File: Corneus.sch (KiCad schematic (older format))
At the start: 145 parts, among them J1 USB_B_Micro, Q1 Q_NPN_BCE, SW1 SW_Push, U1 ATmega32U4-AU, U2 PRTR5V0U2X, Y1 16MHz

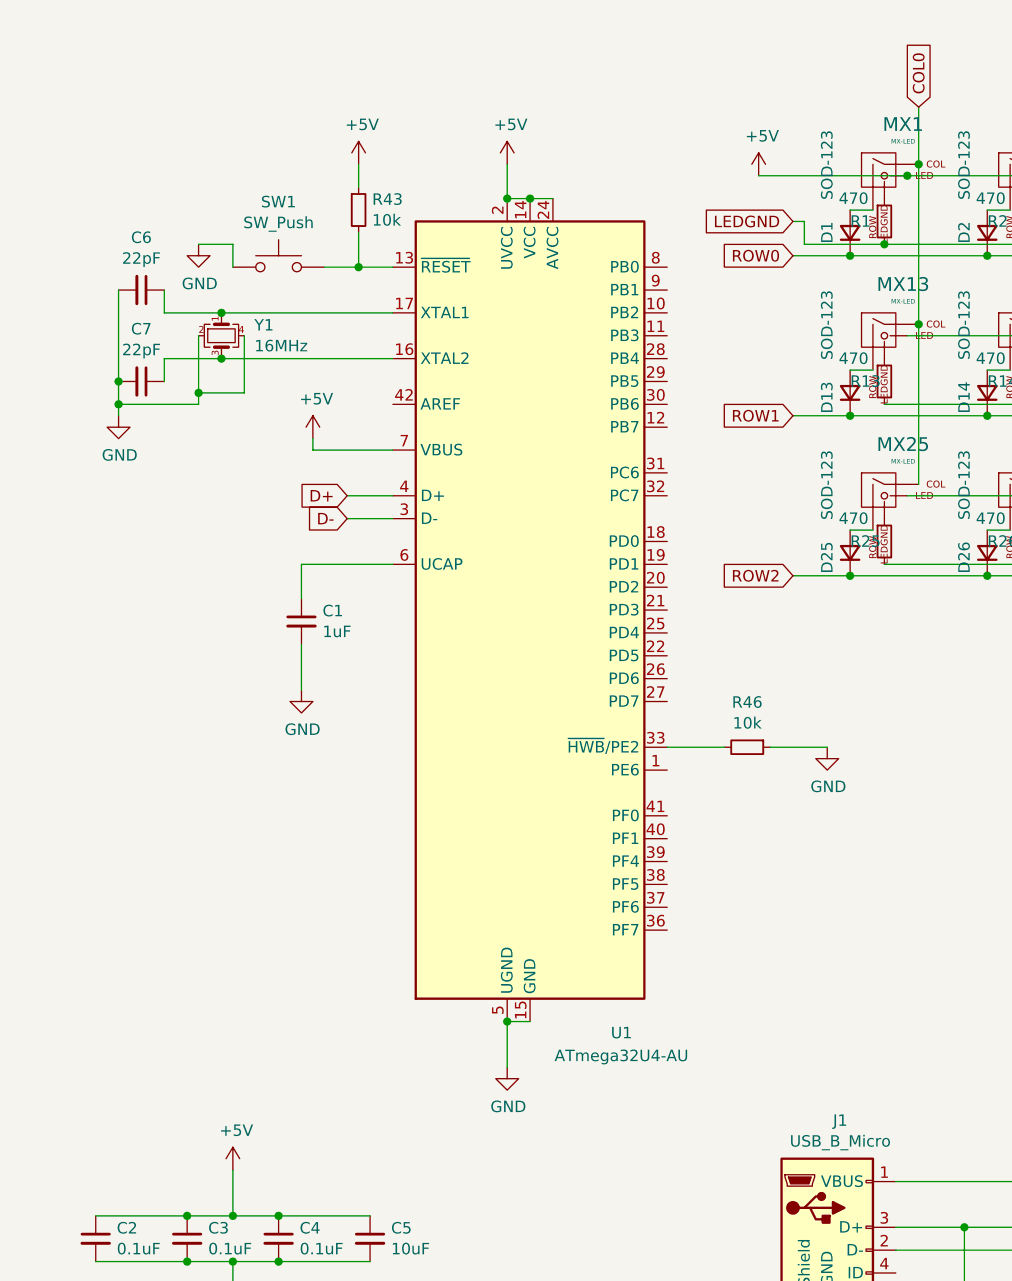
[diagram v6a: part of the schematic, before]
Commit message: routed rows and columns
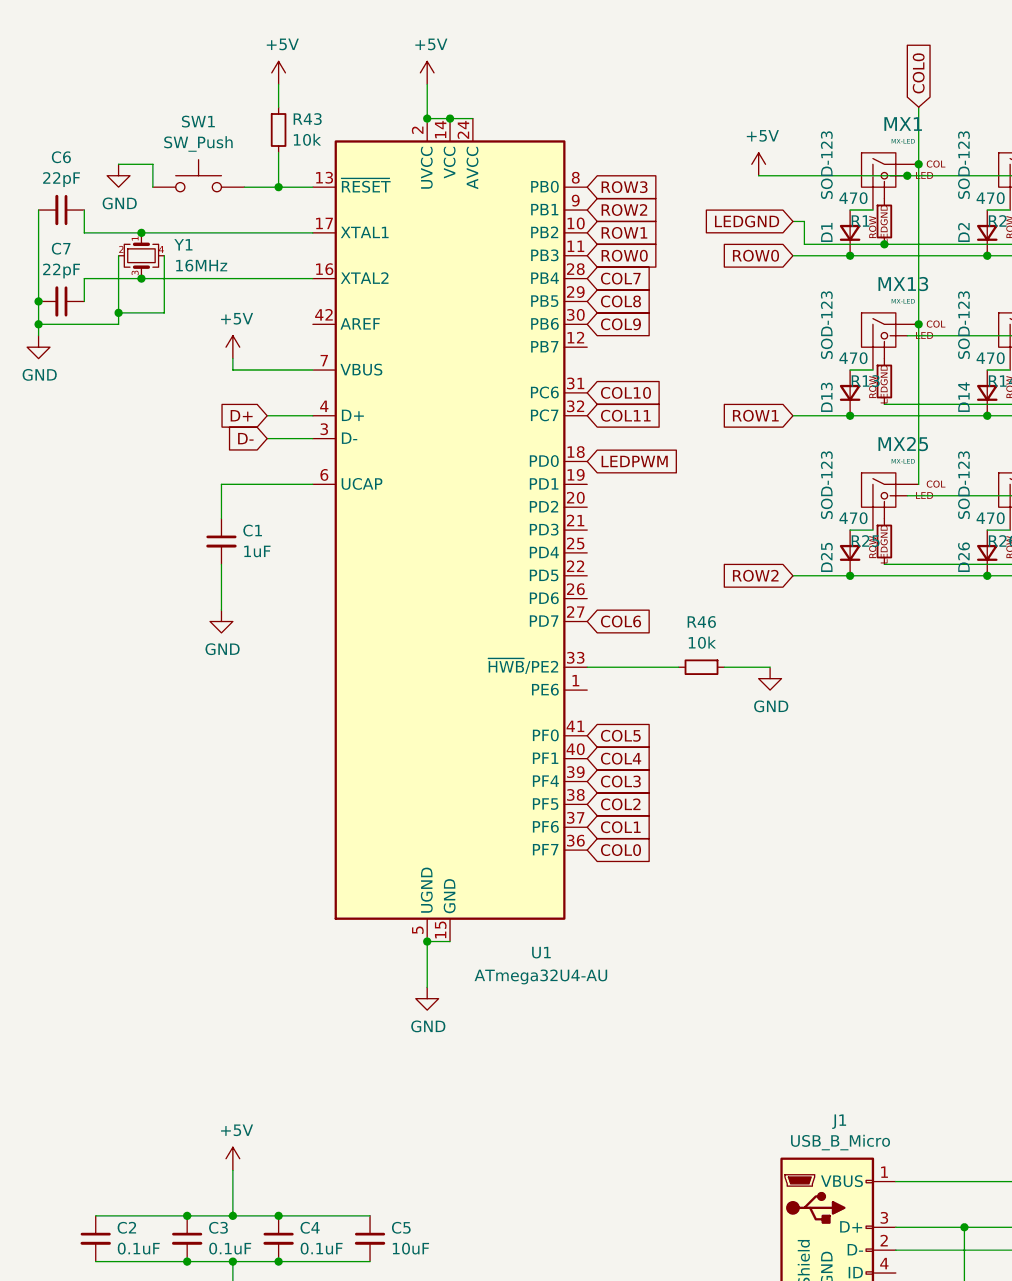
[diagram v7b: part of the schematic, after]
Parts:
- Q1: footprint Package_TO_SOT_SMD:SOT-223 -> digikey-footprints:Trans_SOT-223-4
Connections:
- net COL0: now also U1.36 (PF7)
- net COL1: now also U1.37 (PF6)
- net COL10: now also U1.31 (PC6)
- net COL11: now also U1.32 (PC7)
- net COL2: now also U1.38 (PF5)
- net COL3: now also U1.39 (PF4)
- net COL4: now also U1.40 (PF1)
- net COL5: now also U1.41 (PF0)
- net COL6: now also U1.27 (PD7)
- net COL7: now also U1.28 (PB4)
- net COL8: now also U1.29 (PB5)
- net COL9: now also U1.30 (PB6)
- net LEDPWM: now also U1.18 (PD0)
- net ROW0: now also U1.11 (PB3)
- net ROW1: now also U1.10 (PB2)
- net ROW2: now also U1.9 (PB1)
- net ROW3: now also U1.8 (PB0)
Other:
- moved on the sheet: C1, C6, C7, R43, R46, SW1, U1, Y1

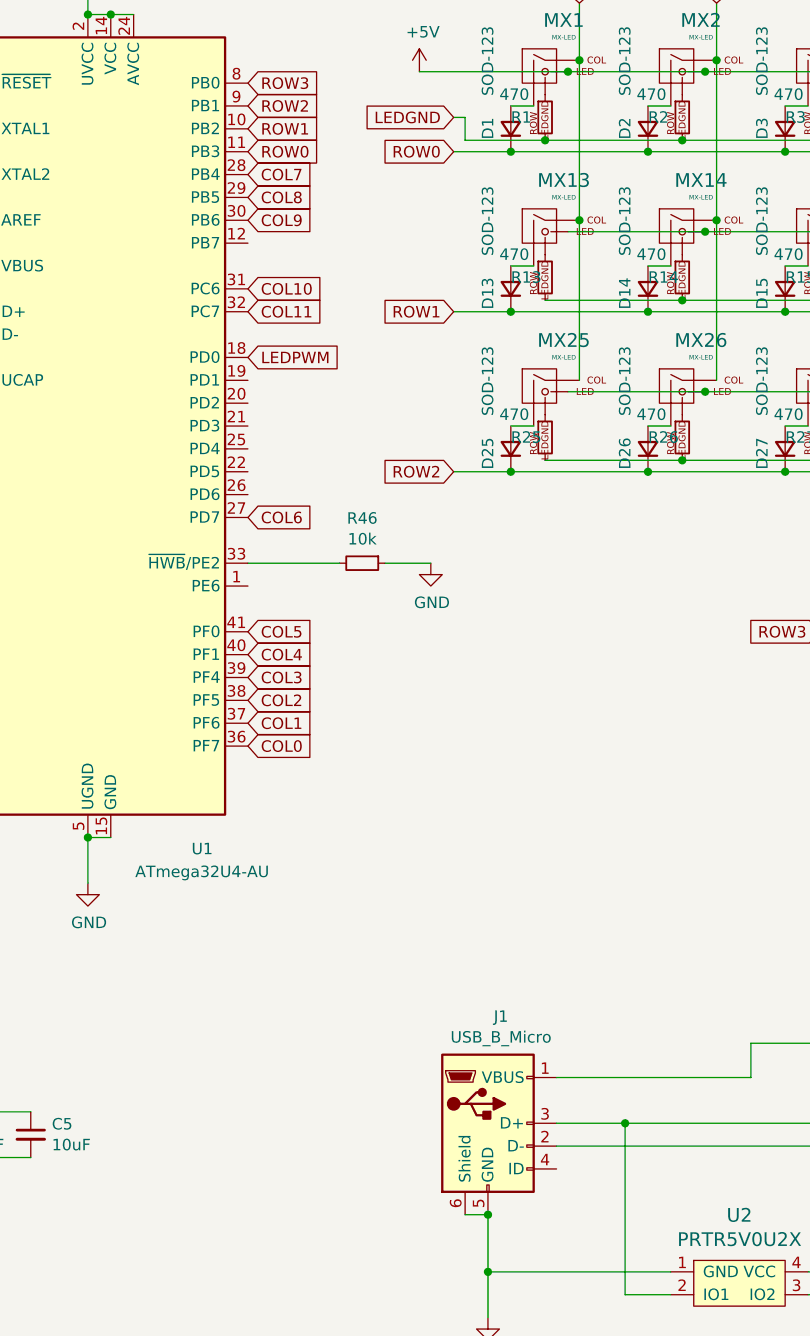
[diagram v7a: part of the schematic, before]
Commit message: rotated MCU region and routed rows
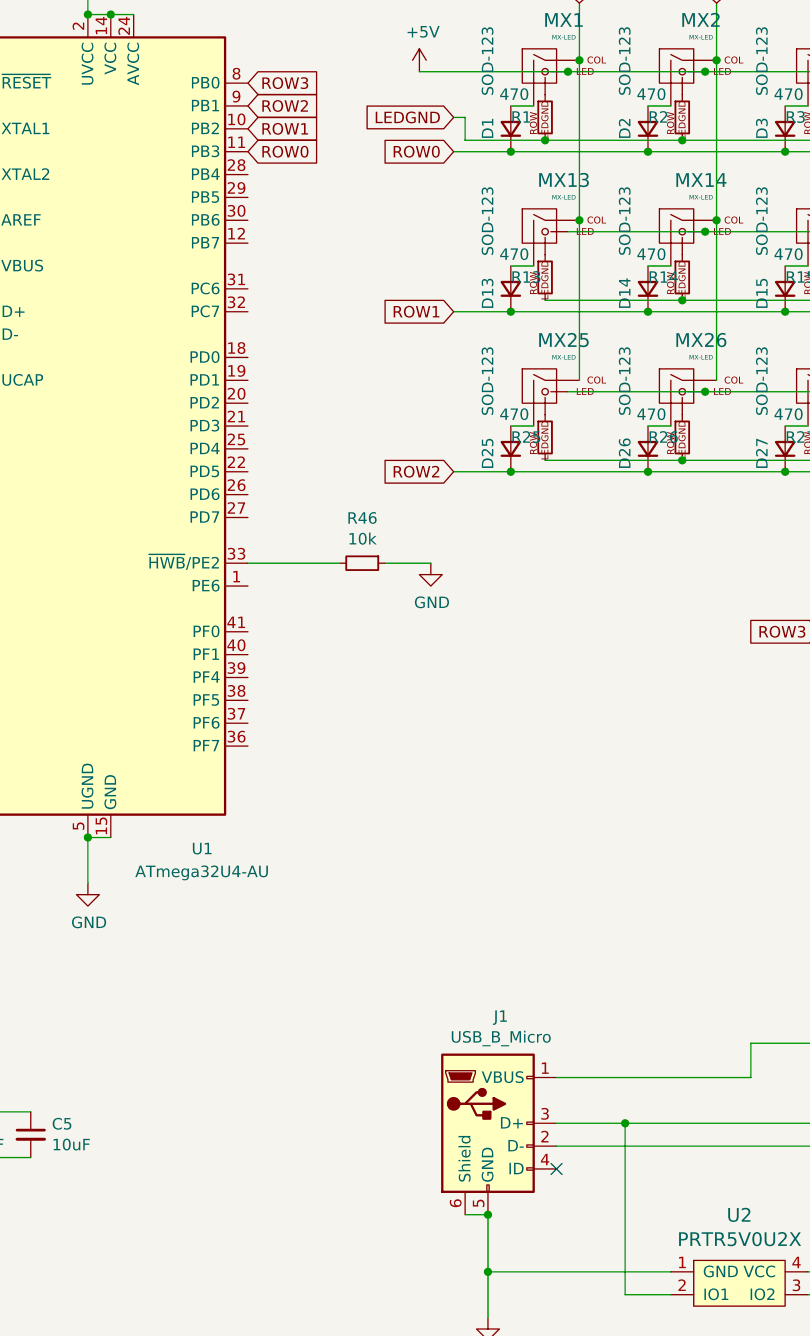
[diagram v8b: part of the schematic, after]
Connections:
- net COL0: no longer U1.36 (PF7)
- net COL1: no longer U1.37 (PF6)
- net COL10: no longer U1.31 (PC6)
- net COL11: no longer U1.32 (PC7)
- net COL2: no longer U1.38 (PF5)
- net COL3: no longer U1.39 (PF4)
- net COL4: no longer U1.40 (PF1)
- net COL5: no longer U1.41 (PF0)
- net COL6: no longer U1.27 (PD7)
- net COL7: no longer U1.28 (PB4)
- net COL8: no longer U1.29 (PB5)
- net COL9: no longer U1.30 (PB6)
- net LEDPWM: no longer U1.18 (PD0)
- no-connect marks 0 -> 1
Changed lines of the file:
@@
 	3900 6100 4000 6100
 Connection ~ 4000 6100
-Text GLabel 2950 2350 2    50   Input ~ 0
-LEDPWM
-Text GLabel 2950 2150 2    50   Input ~ 0
-COL11
-Text GLabel 2950 2050 2    50   Input ~ 0
-COL10
-Text GLabel 2950 1750 2    50   Input ~ 0
-COL9
-Text GLabel 2950 1650 2    50   Input ~ 0
-COL8
-Text GLabel 2950 1550 2    50   Input ~ 0
-COL7
-Text GLabel 2950 3050 2    50   Input ~ 0
-COL6
-Text GLabel 2950 4050 2    50   Input ~ 0
-COL0
-Text GLabel 2950 3950 2    50   Input ~ 0
-COL1
-Text GLabel 2950 3850 2    50   Input ~ 0
-COL2
-Text GLabel 2950 3750 2    50   Input ~ 0
-COL3
-Text GLabel 2950 3650 2    50   Input ~ 0
-COL4
-Text GLabel 2950 3550 2    50   Input ~ 0
-COL5
+NoConn ~ 4300 5900
 Text GLabel 2950 1150 2    50   Input ~ 0
 ROW3
